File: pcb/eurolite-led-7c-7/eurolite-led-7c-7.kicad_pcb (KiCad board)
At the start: 2 copper layers, 19 parts, among them J2 Conn_01x04, J3 USB_C_Receptacle, SW1 PTS526_SM15_SMTR2_LFS, SW2 PTS526_SM15_SMTR2_LFS, U1 ESP32-S3-MINI-1U, U2 IP4234CZ6, U3 ADP2108AUJ-3.3, U4 ST485E

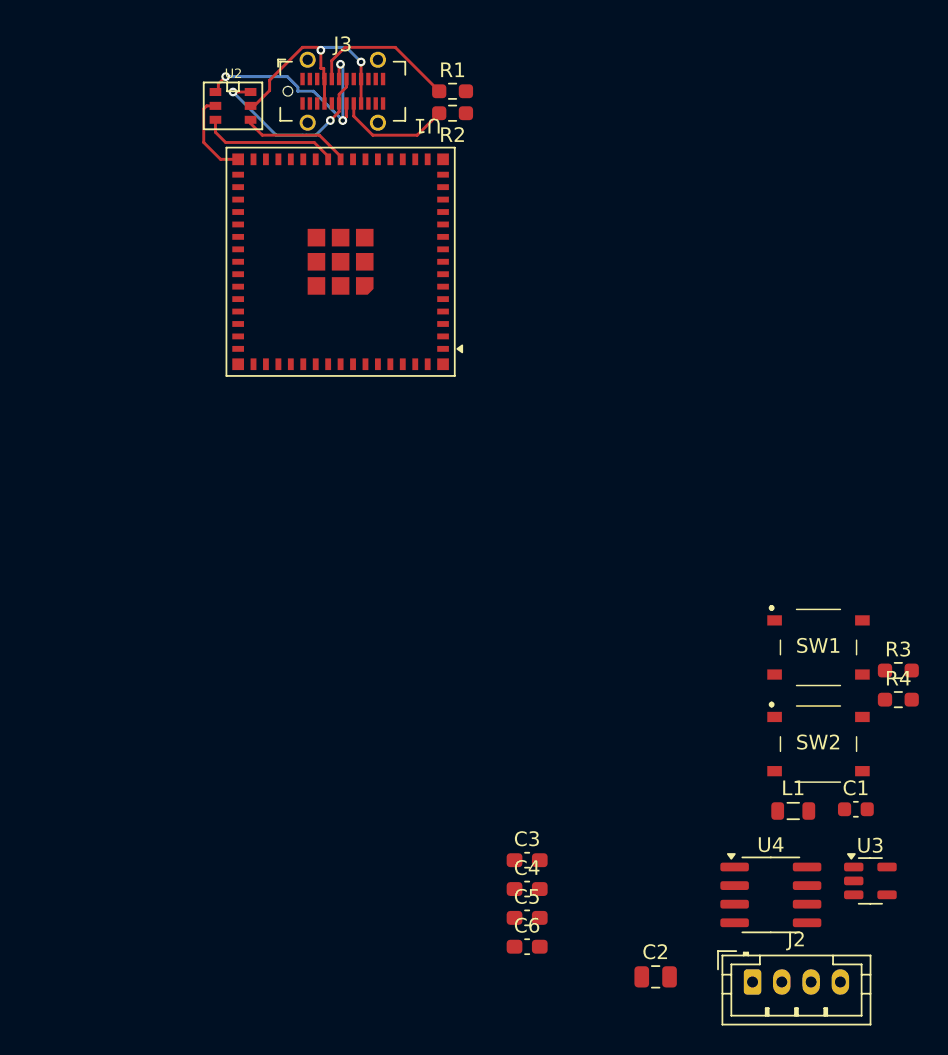
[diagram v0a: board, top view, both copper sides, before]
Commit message: adding current project status
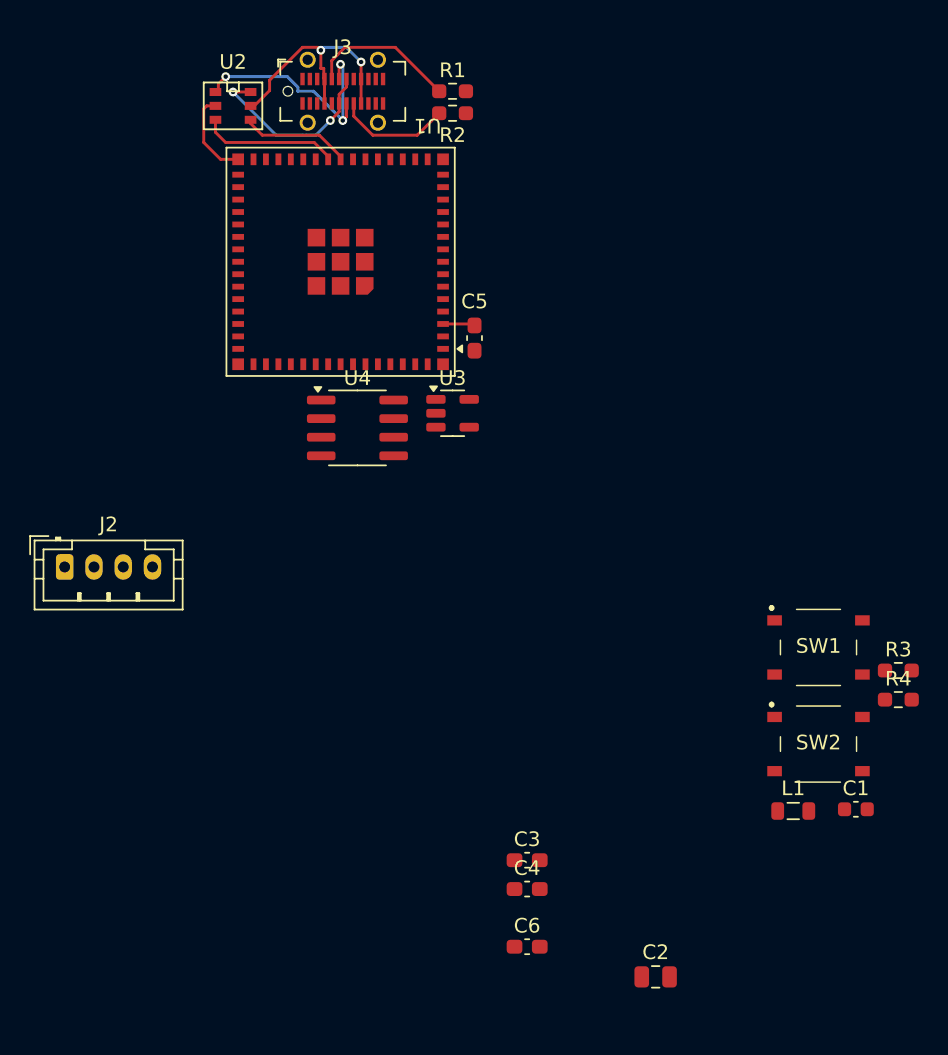
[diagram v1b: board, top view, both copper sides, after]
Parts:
- moved J2 54.9 mm to (131.0, 82.5)
- moved U3 42.8 mm to (157.5, 72.0)
- moved U4 42.6 mm to (151.0, 73.0)
- moved C5 39.8 mm to (159.0, 66.9), turned to -90 degrees
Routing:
- net VCC_3.3V: track 0.00 -> 2.25 mm
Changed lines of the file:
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@@
 	(footprint "Package_SO:SOIC-8_3.9x4.9mm_P1.27mm"
 		(layer "F.Cu")
-		(at 179.245 104.905)
+		(at 151 73)
 		(descr "SOIC, 8 Pin (JEDEC MS-012AA, https://www.analog.com/media/en/package-pcb-resources/package/pkg_pdf/soic_narrow-r/r_8.pdf), generated with kicad-footprint-generator ipc_gullwing_generator.py")
 		(tags "SOIC SO")
@@
 		(at 142.5 51)
 		(property "Reference" "U2"
-			(at 0.032 -2.2064 0)
+			(at 0 -3 0)
 			(layer "F.SilkS")
 			(effects
 				(font
-					(size 0.64 0.64)
+					(size 1 1)
 					(thickness 0.15)
 				)
@@
 	(footprint "Package_TO_SOT_SMD:TSOT-23-5"
 		(layer "F.Cu")
-		(at 186.045 103.95)
+		(at 157.5 72)
 		(descr "TSOT, 5 Pin (https://www.jedec.org/sites/default/files/docs/MO-193D.pdf variant AB), generated with kicad-footprint-generator ipc_gullwing_generator.py")
 		(tags "TSOT TO_SOT_SMD")
@@
 	(footprint "Capacitor_SMD:C_0603_1608Metric_Pad1.08x0.95mm_HandSolder"
 		(layer "F.Cu")
-		(at 162.595 106.475)
+		(at 159 66.8625 -90)
 		(descr "Capacitor SMD 0603 (1608 Metric), square (rectangular) end terminal, IPC-7351 nominal with elongated pad for handsoldering. (Body size source: IPC-SM-782 page 76, https://www.pcb-3d.com/wordpress/wp-content/uploads/ipc-sm-782a_amendment_1_and_2.pdf), generated with kicad-footprint-generator")
 		(tags "capacitor handsolder")
 		(property "Reference" "C5"
-			(at 0 -1.43 0)
+			(at -2.5 0 0)
 			(layer "F.SilkS")
 			(effects
@@
 		)
 		(property "Value" "0u1F"
-			(at 0 1.43 0)
+			(at 0 -3 180)
 			(layer "F.Fab")
 			(effects
@@
 		)
 		(property "Datasheet" ""
-			(at 0 0 0)
+			(at 0 0 90)
 			(layer "F.Fab")
 			(hide yes)
@@
 		)
 		(property "Description" "Unpolarized capacitor"
-			(at 0 0 0)
+			(at 0 0 90)
 			(layer "F.Fab")
 			(hide yes)
@@
 		)
 		(property "MOUSER_PART_NUMBER" "187-CL05F104ZO5NNND"
-			(at 0 0 0)
+			(at 0 0 270)
 			(unlocked yes)
 			(layer "F.Fab")
@@
 		(attr smd)
 		(fp_line
-			(start -0.146267 -0.51)
-			(end 0.146267 -0.51)
+			(start -0.146267 0.51)
+			(end 0.146267 0.51)
 			(stroke
 				(width 0.12)
@@
 		)
 		(fp_line
-			(start -0.146267 0.51)
-			(end 0.146267 0.51)
+			(start -0.146267 -0.51)
+			(end 0.146267 -0.51)
 			(stroke
 				(width 0.12)
@@
 		)
 		(fp_line
-			(start -1.65 -0.73)
-			(end 1.65 -0.73)
+			(start -1.65 0.73)
+			(end -1.65 -0.73)
 			(stroke
 				(width 0.05)
@@
 		)
 		(fp_line
-			(start -1.65 0.73)
-			(end -1.65 -0.73)
+			(start 1.65 0.73)
+			(end -1.65 0.73)
 			(stroke
 				(width 0.05)
@@
 		)
 		(fp_line
-			(start 1.65 -0.73)
-			(end 1.65 0.73)
+			(start -1.65 -0.73)
+			(end 1.65 -0.73)
 			(stroke
 				(width 0.05)
@@
 		)
 		(fp_line
-			(start 1.65 0.73)
-			(end -1.65 0.73)
+			(start 1.65 -0.73)
+			(end 1.65 0.73)
 			(stroke
 				(width 0.05)
@@
 		)
 		(fp_line
-			(start -0.8 -0.4)
-			(end 0.8 -0.4)
+			(start -0.8 0.4)
+			(end -0.8 -0.4)
 			(stroke
 				(width 0.1)
@@
 		)
 		(fp_line
-			(start -0.8 0.4)
-			(end -0.8 -0.4)
+			(start 0.8 0.4)
+			(end -0.8 0.4)
 			(stroke
 				(width 0.1)
@@
 		)
 		(fp_line
-			(start 0.8 -0.4)
-			(end 0.8 0.4)
+			(start -0.8 -0.4)
+			(end 0.8 -0.4)
 			(stroke
 				(width 0.1)
@@
 		)
 		(fp_line
-			(start 0.8 0.4)
-			(end -0.8 0.4)
+			(start 0.8 -0.4)
+			(end 0.8 0.4)
 			(stroke
 				(width 0.1)
@@
 		)
 		(fp_text user "${REFERENCE}"
-			(at 0 0 0)
+			(at 0 0 90)
 			(layer "F.Fab")
 			(effects
@@
 		)
 		(pad "1" smd roundrect
-			(at -0.8625 0)
+			(at -0.8625 0 270)
 			(size 1.075 0.95)
 			(layers "F.Cu" "F.Mask" "F.Paste")
@@
 		)
 		(pad "2" smd roundrect
-			(at 0.8625 0)
+			(at 0.8625 0 270)
 			(size 1.075 0.95)
 			(layers "F.Cu" "F.Mask" "F.Paste")
@@
 		(tags "USB C Type-C Receptacle SMD")
 		(property "Reference" "J3"
-			(at 0 -3.2 0)
+			(at 0 -3 0)
 			(layer "F.SilkS")
 			(effects
@@
 	(footprint "Connector_JST:JST_PH_B4B-PH-K_1x04_P2.00mm_Vertical"
 		(layer "F.Cu")
-		(at 177.995 110.855)
+		(at 131 82.5)
 		(descr "JST PH series connector, B4B-PH-K (http://www.jst-mfg.com/product/pdf/eng/ePH.pdf), generated with kicad-footprint-generator")
 		(tags "connector JST PH vertical")
@@
 	)
 	(segment
+		(start 159 66.1375)
+		(end 158.7625 65.9)
+		(width 0.2)
+		(layer "F.Cu")
+		(net 30)
+	)
+	(segment
+		(start 158.7625 65.9)
+		(end 156.85 65.9)
+		(width 0.2)
+		(layer "F.Cu")
+		(net 30)
+	)
+	(segment
